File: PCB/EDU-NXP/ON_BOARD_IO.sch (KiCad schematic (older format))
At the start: 56 parts, among them Q1 2N7000, Q10 2N7000, Q11 2N7000, Q12 2N7000, Q2 2N7000, Q3 2N7000, Q4 2N7000, Q5 2N7000, Q6 2N7000, Q7 2N7000, Q8 2N7000, Q9 2N7000, SW2 SW_PUSH, SW3 SW_PUSH, SW4 SW_PUSH, SW5 SW_PUSH

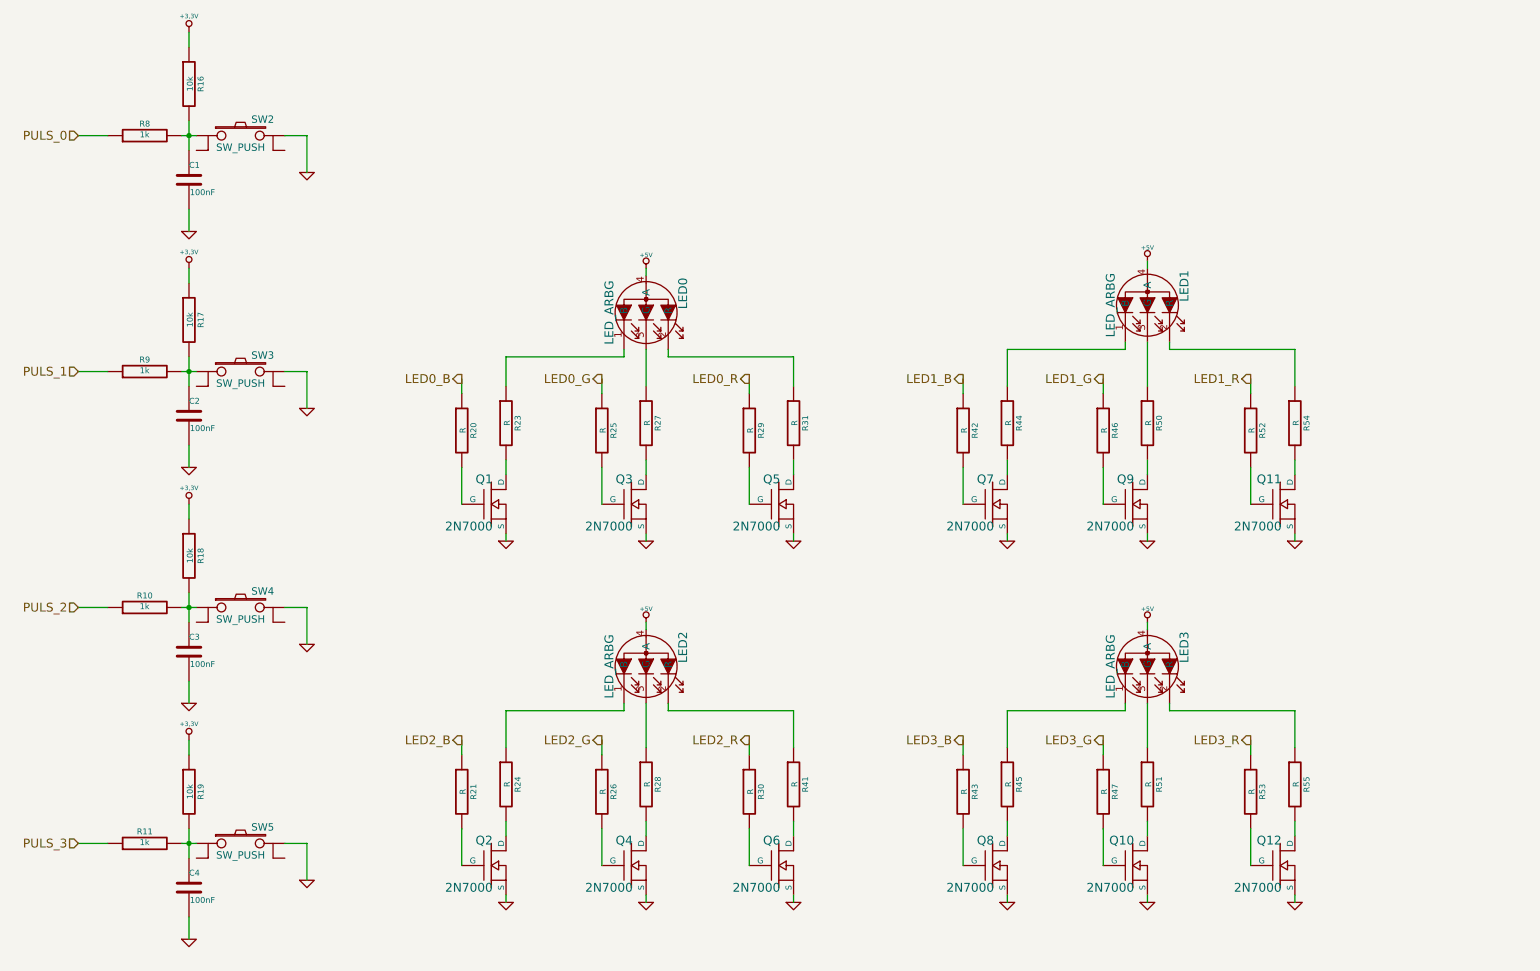
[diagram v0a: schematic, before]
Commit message: Versión completa del esquemático con todos los componentes ya definidos
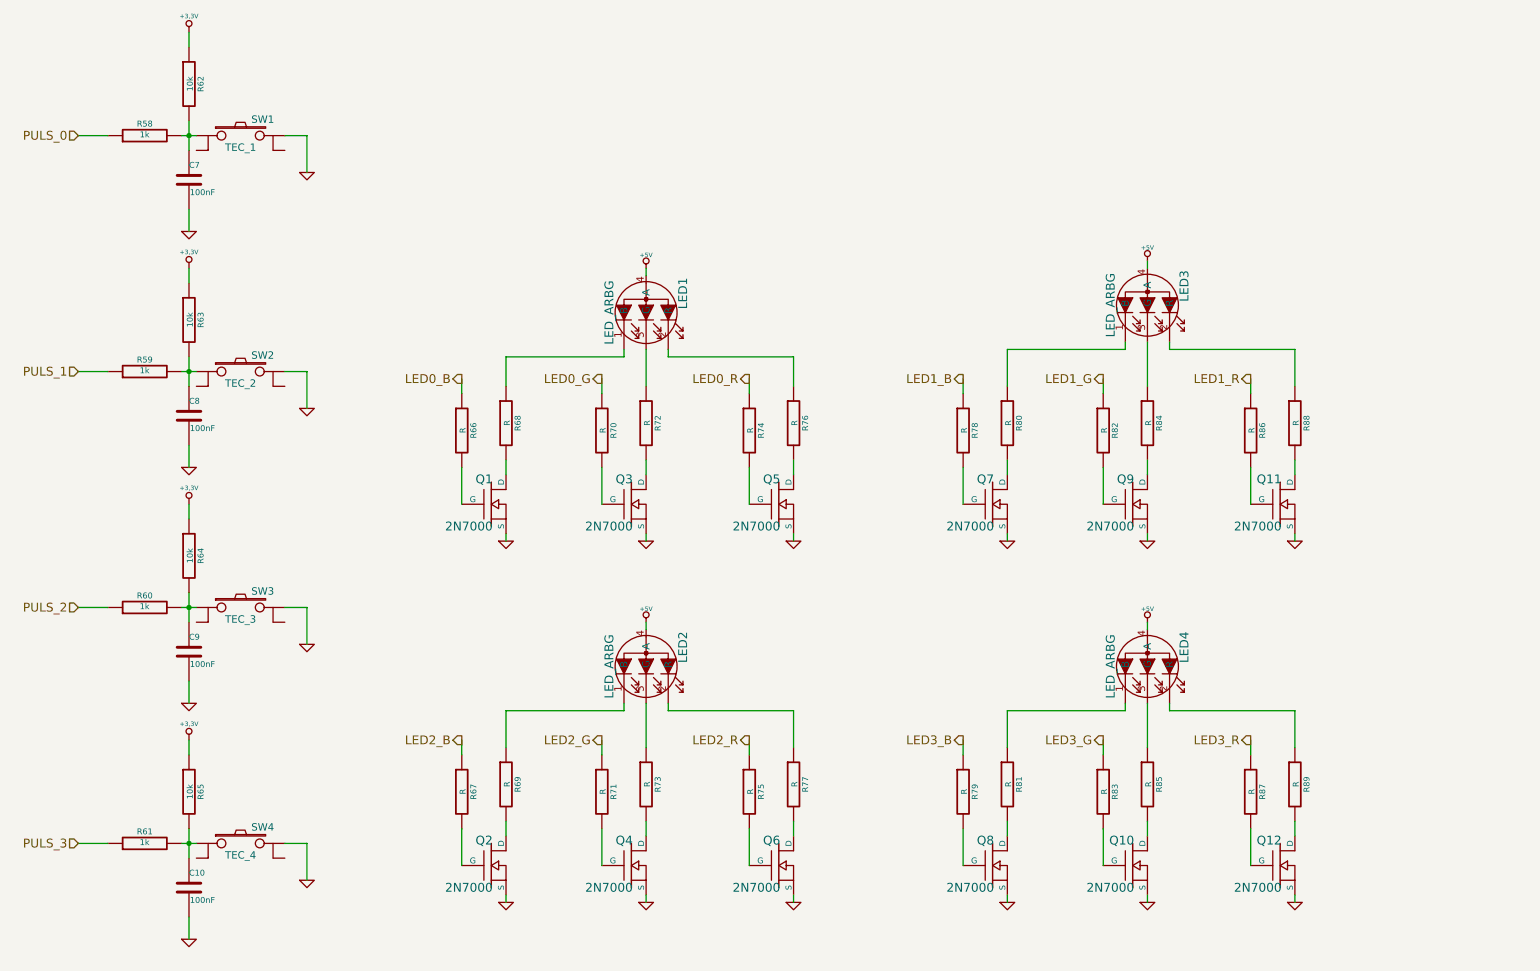
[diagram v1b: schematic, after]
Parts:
- SW1: renamed from SW2; value SW_PUSH -> TEC_1
- SW2: renamed from SW3; value SW_PUSH -> TEC_2
- SW3: renamed from SW4; value SW_PUSH -> TEC_3
- SW4: renamed from SW5; value SW_PUSH -> TEC_4
- renumbered C4 to C10, C1 to C7, C2 to C8, C3 to C9, LED0 to LED1, LED1 to LED3, LED3 to LED4, R8 to R58, R9 to R59, R10 to R60, R11 to R61, R16 to R62, R17 to R63, R18 to R64, R19 to R65, R20 to R66, R21 to R67, R23 to R68, R24 to R69, R25 to R70, R26 to R71, R27 to R72, R28 to R73, R29 to R74, R30 to R75, R31 to R76, R41 to R77, R42 to R78, R43 to R79, R44 to R80, R45 to R81, R46 to R82, R47 to R83, R50 to R84, R51 to R85, R52 to R86, R53 to R87, R54 to R88, R55 to R89

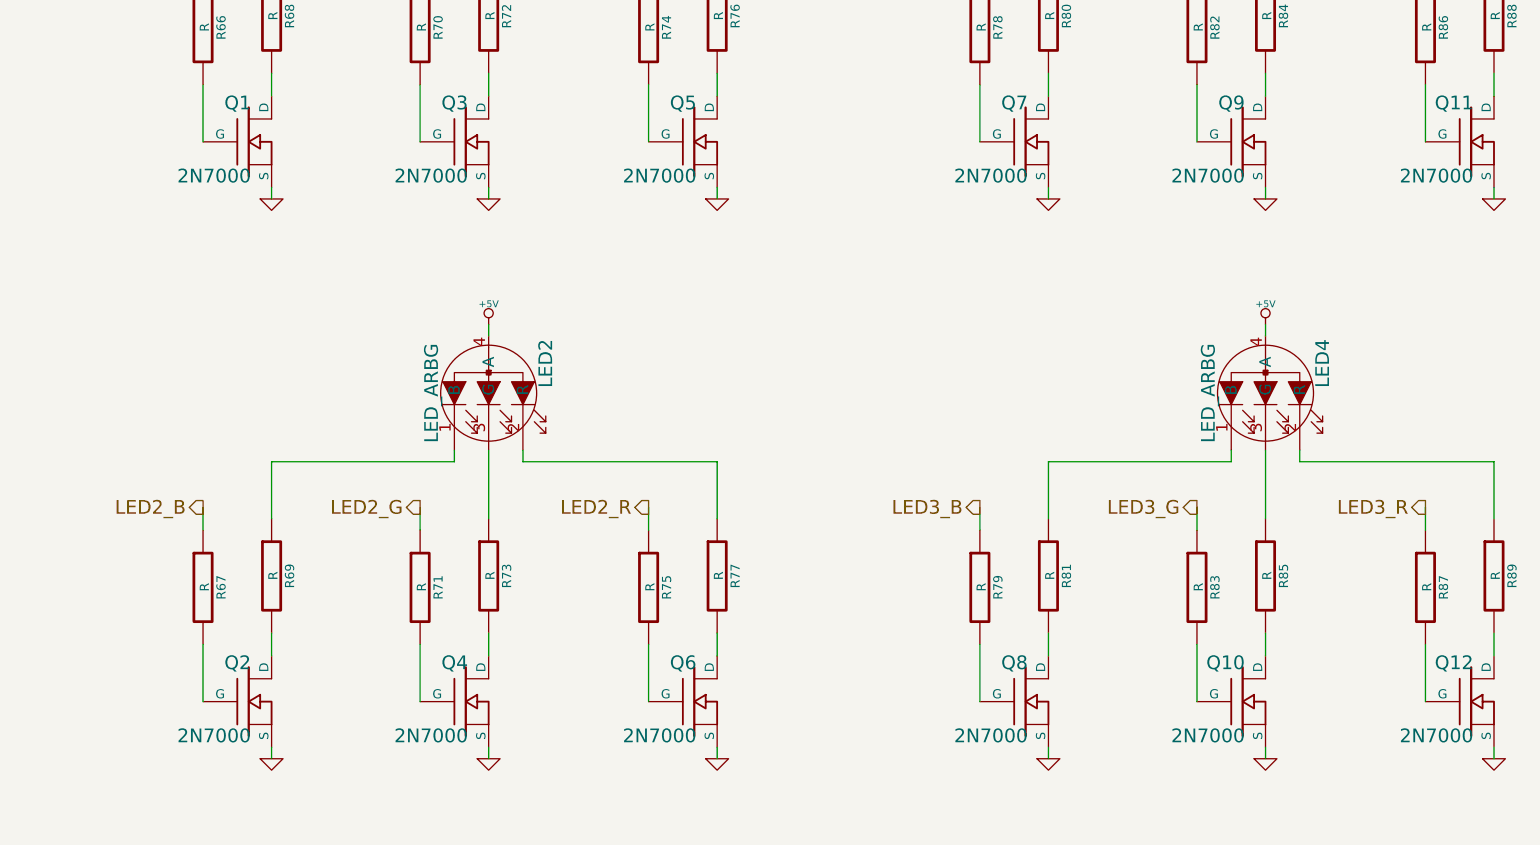
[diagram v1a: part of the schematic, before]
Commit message: El PCB tiene el tamaño de la CIAA-NXP y se colocaron los componentes en una distribución provisoria
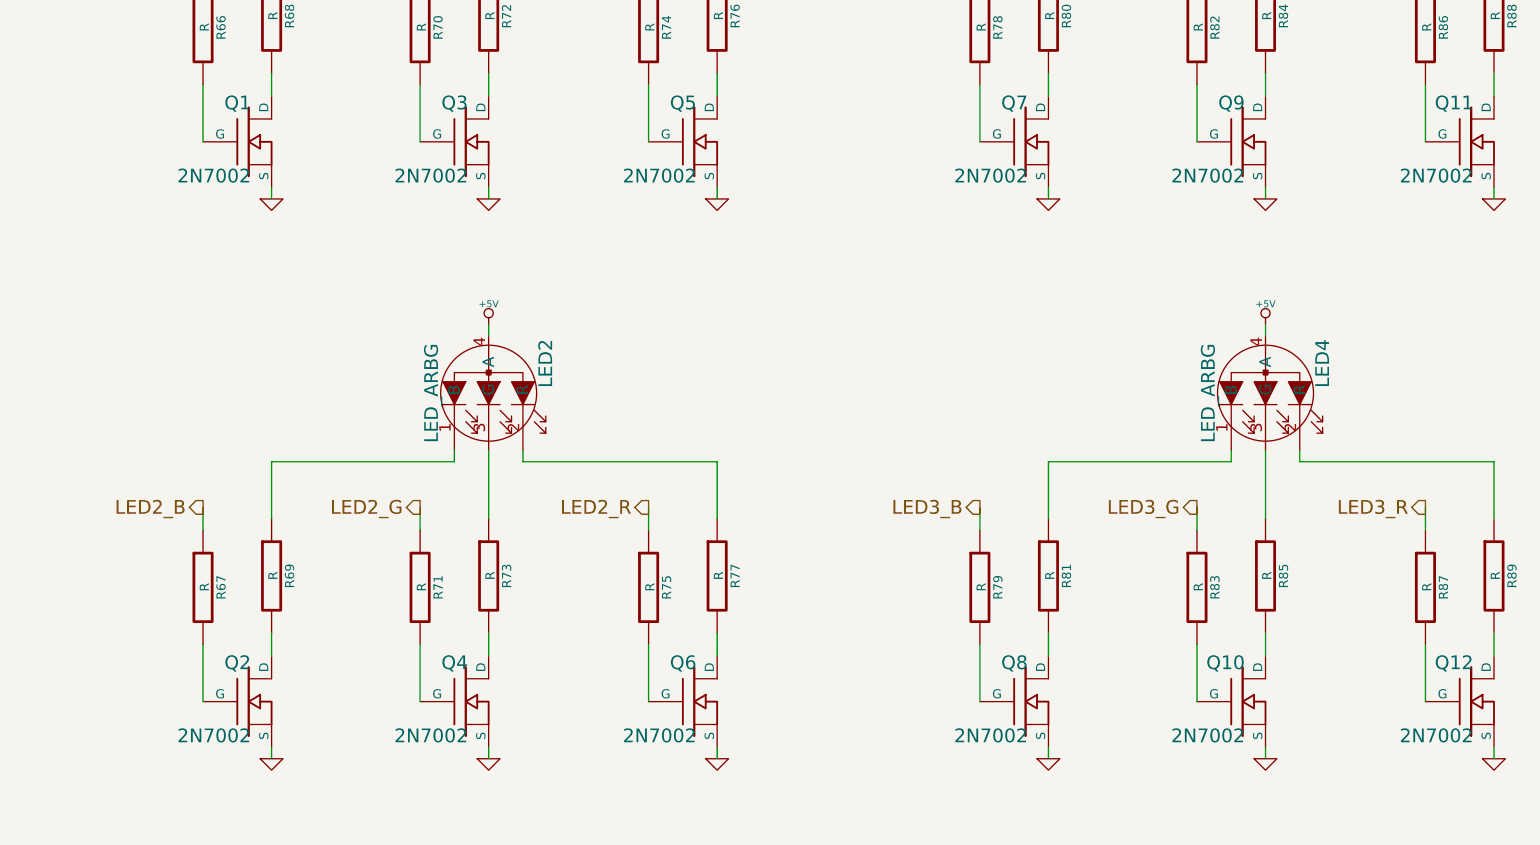
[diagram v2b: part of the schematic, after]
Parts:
- Q1, Q10, Q11, Q12, Q2, Q3, Q4, Q5, Q6, Q7, Q8, Q9: value 2N7000 -> 2N7002
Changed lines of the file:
@@
 Sheet 6 7
 Title "EDU CIAA EXPANSIÓN"
-Date "24 jun 2014"
+Date "27 jun 2014"
 Rev ""
 Comp ""
@@
 P 7350 3900
 F 0 "Q7" H 7360 4070 60  0000 R CNN
-F 1 "2N7000" H 7360 3750 60  0000 R CNN
+F 1 "2N7002" H 7360 3750 60  0000 R CNN
 F 2 "~" H 7350 3900 60  0000 C CNN
 F 3 "~" H 7350 3900 60  0000 C CNN
@@
 P 8300 3900
 F 0 "Q9" H 8310 4070 60  0000 R CNN
-F 1 "2N7000" H 8310 3750 60  0000 R CNN
+F 1 "2N7002" H 8310 3750 60  0000 R CNN
 F 2 "~" H 8300 3900 60  0000 C CNN
 F 3 "~" H 8300 3900 60  0000 C CNN
@@
 P 9300 3900
 F 0 "Q11" H 9310 4070 60  0000 R CNN
-F 1 "2N7000" H 9310 3750 60  0000 R CNN
+F 1 "2N7002" H 9310 3750 60  0000 R CNN
 F 2 "~" H 9300 3900 60  0000 C CNN
 F 3 "~" H 9300 3900 60  0000 C CNN
@@
 P 7350 6350
 F 0 "Q8" H 7360 6520 60  0000 R CNN
-F 1 "2N7000" H 7360 6200 60  0000 R CNN
+F 1 "2N7002" H 7360 6200 60  0000 R CNN
 F 2 "~" H 7350 6350 60  0000 C CNN
 F 3 "~" H 7350 6350 60  0000 C CNN
@@
 P 8300 6350
 F 0 "Q10" H 8310 6520 60  0000 R CNN
-F 1 "2N7000" H 8310 6200 60  0000 R CNN
+F 1 "2N7002" H 8310 6200 60  0000 R CNN
 F 2 "~" H 8300 6350 60  0000 C CNN
 F 3 "~" H 8300 6350 60  0000 C CNN
@@
 P 9300 6350
 F 0 "Q12" H 9310 6520 60  0000 R CNN
-F 1 "2N7000" H 9310 6200 60  0000 R CNN
+F 1 "2N7002" H 9310 6200 60  0000 R CNN
 F 2 "~" H 9300 6350 60  0000 C CNN
 F 3 "~" H 9300 6350 60  0000 C CNN
@@
 P 3950 3900
 F 0 "Q1" H 3960 4070 60  0000 R CNN
-F 1 "2N7000" H 3960 3750 60  0000 R CNN
+F 1 "2N7002" H 3960 3750 60  0000 R CNN
 F 2 "~" H 3950 3900 60  0000 C CNN
 F 3 "~" H 3950 3900 60  0000 C CNN
@@
 P 4900 3900
 F 0 "Q3" H 4910 4070 60  0000 R CNN
-F 1 "2N7000" H 4910 3750 60  0000 R CNN
+F 1 "2N7002" H 4910 3750 60  0000 R CNN
 F 2 "~" H 4900 3900 60  0000 C CNN
 F 3 "~" H 4900 3900 60  0000 C CNN
@@
 P 5900 3900
 F 0 "Q5" H 5910 4070 60  0000 R CNN
-F 1 "2N7000" H 5910 3750 60  0000 R CNN
+F 1 "2N7002" H 5910 3750 60  0000 R CNN
 F 2 "~" H 5900 3900 60  0000 C CNN
 F 3 "~" H 5900 3900 60  0000 C CNN
@@
 P 3950 6350
 F 0 "Q2" H 3960 6520 60  0000 R CNN
-F 1 "2N7000" H 3960 6200 60  0000 R CNN
+F 1 "2N7002" H 3960 6200 60  0000 R CNN
 F 2 "~" H 3950 6350 60  0000 C CNN
 F 3 "~" H 3950 6350 60  0000 C CNN
@@
 P 4900 6350
 F 0 "Q4" H 4910 6520 60  0000 R CNN
-F 1 "2N7000" H 4910 6200 60  0000 R CNN
+F 1 "2N7002" H 4910 6200 60  0000 R CNN
 F 2 "~" H 4900 6350 60  0000 C CNN
 F 3 "~" H 4900 6350 60  0000 C CNN
@@
 P 5900 6350
 F 0 "Q6" H 5910 6520 60  0000 R CNN
-F 1 "2N7000" H 5910 6200 60  0000 R CNN
+F 1 "2N7002" H 5910 6200 60  0000 R CNN
 F 2 "~" H 5900 6350 60  0000 C CNN
 F 3 "~" H 5900 6350 60  0000 C CNN

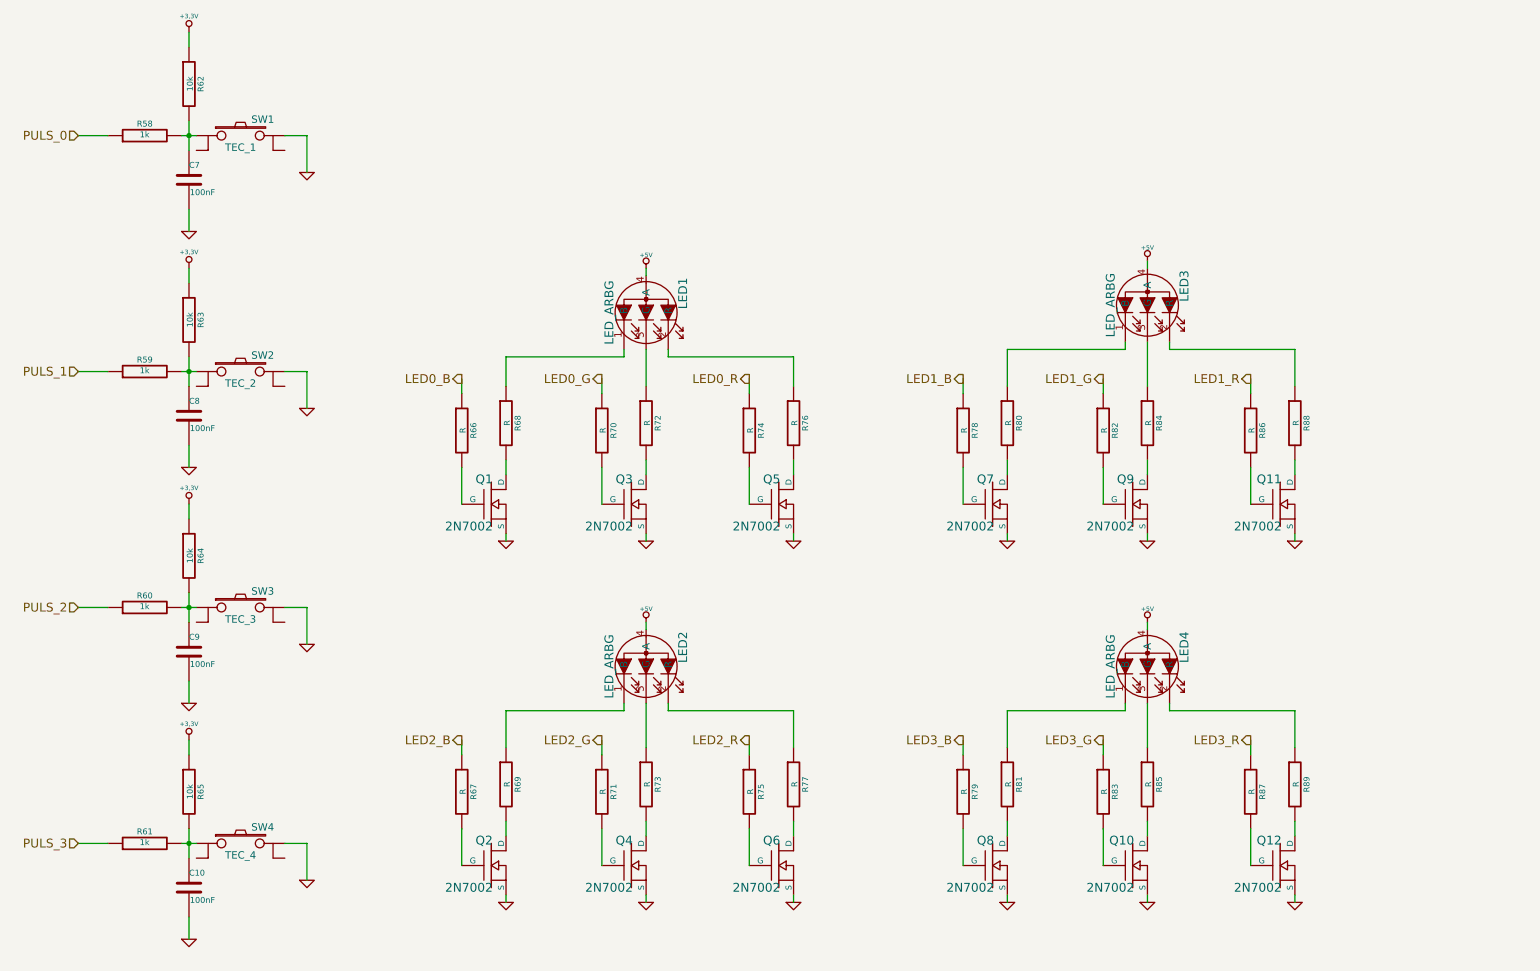
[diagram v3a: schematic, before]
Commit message: Se cambiaron los leds - Avances sobre el ruteo del PCB
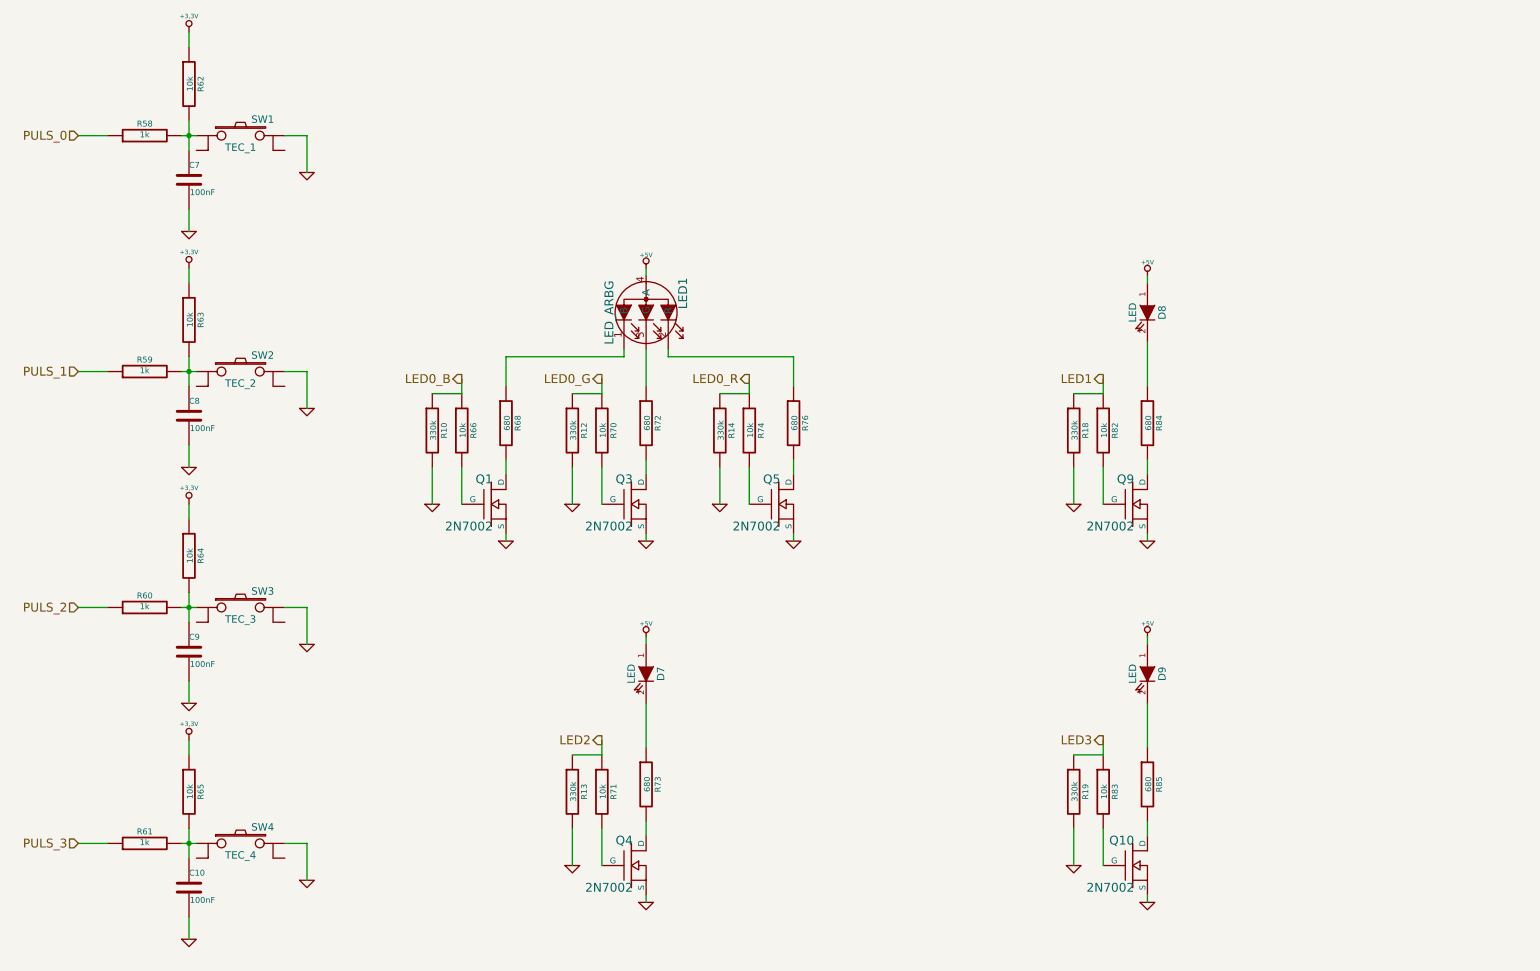
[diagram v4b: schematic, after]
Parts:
- removed LED2, LED3, LED4: LED_ARBG, symbol LED_ARBG
- removed Q11, Q12, Q2, Q6, Q7, Q8: 2N7002, ~, symbol MOSFET_N
- removed R67, R69, R75, R77, R78, R79, R80, R81, R86, R87, R88, R89: R, ~, symbol R
- added D7, D8, D9: LED, ~, symbol LED
- added R10, R12, R13, R14, R18, R19: 330k, ~, symbol R
- R66, R70, R71, R74, R82, R83: value R -> 10k
- R68, R72, R73, R76, R84, R85: value R -> 680
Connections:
- net +5V: now also D7.1 (A), D8.1 (A), D9.1 (A)
- net GND: now also R10.2, R12.2, R13.2, R14.2, R18.2, R19.2
- net LED0_B: now also R10.1
- net LED0_G: now also R12.1
- net LED0_R: now also R14.1
- net at R84.1: now also D8.2 (K)
- net at R73.1: now also D7.2 (K)
- net at R85.1: now also D9.2 (K)
- net LED1_G renamed LED1
- net LED1: now also R18.1
- net LED2_G renamed LED2
- net LED2: now also R13.1
- net LED3_G renamed LED3
- net LED3: now also R19.1
